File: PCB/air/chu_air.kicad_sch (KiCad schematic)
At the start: 24 parts, among them J1 Conn_01x06_Socket, Q1 Q_Photo_NPN, Q2 Q_Photo_NPN, Q3 Q_Photo_NPN, Q4 Q_Photo_NPN, Q5 Q_Photo_NPN, Q6 Q_Photo_NPN

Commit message: Another attempt of chu air
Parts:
- removed D10, D11, D12, D4, D5, D6, D7, D8, D9: IR26-21C_L110_TR8, LED_SMD:LED_1206_3216Metric_Pad1.42x1.75mm_HandSolder, symbol LED:IR26-21C_L110_TR8
- removed Q4, Q5, Q6: Q_Photo_NPN, LED_SMD:LED_1206_3216Metric_Pad1.42x1.75mm_HandSolder, symbol Device:Q_Photo_NPN
- removed R2: R, Resistor_SMD:R_0805_2012Metric_Pad1.20x1.40mm_HandSolder, symbol Device:R
- added J2: Conn_01x06_Socket, chu_air:6P_Air_Conn, symbol Connector:Conn_01x06_Socket
- added Q1, Q3, Q5: AO3400A, Package_TO_SOT_SMD:SOT-23, symbol Transistor_FET:AO3400A
- added R2, R4, R6: 1R, Resistor_SMD:R_0603_1608Metric, symbol Device:R_Small
- D1, D2, D3: footprint LED_SMD:LED_1206_3216Metric_Pad1.42x1.75mm_HandSolder -> LED_THT:LED_D5.0mm_IRGrey
- Q2: renamed from Q1; footprint LED_SMD:LED_1206_3216Metric_Pad1.42x1.75mm_HandSolder -> LED_THT:LED_D5.0mm_IRBlack
- Q4: renamed from Q2; footprint LED_SMD:LED_1206_3216Metric_Pad1.42x1.75mm_HandSolder -> LED_THT:LED_D5.0mm_IRBlack
- Q6: renamed from Q3; footprint LED_SMD:LED_1206_3216Metric_Pad1.42x1.75mm_HandSolder -> LED_THT:LED_D5.0mm_IRBlack
- R1, R3, R5: value R -> 10R; footprint Resistor_SMD:R_0805_2012Metric_Pad1.20x1.40mm_HandSolder -> Resistor_SMD:R_0603_1608Metric
- R7: renamed from R4; value R -> 10K; footprint Resistor_SMD:R_0805_2012Metric_Pad1.20x1.40mm_HandSolder -> Resistor_SMD:R_0603_1608Metric
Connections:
- net A: now also J2.1 (Pin_1)
- net B: now also J2.2 (Pin_2)
- net C: now also R5.1, J2.3 (Pin_3)
- net GND: now also J1.6 (Pin_6), J2.6 (Pin_6), Q1.2 (S), Q3.2 (S), Q5.2 (S); no longer J1.5 (Pin_5), R5.2
- net at R3.2: now also Q3.1 (G)
- net +3.3V: now reaches D3.2 (A)
- net +3.3V: now also D1.2 (A), D2.2 (A), J1.4 (Pin_4), J2.4 (Pin_4)
- net at D3.1 (K): now also R6.2
- net at D1.1 (K): now also R2.2
- net AD1 renamed SIG
- net SIG: now also J1.5 (Pin_5), J2.5 (Pin_5); no longer J1.6 (Pin_6)
- removed net AD2: J1.4 (Pin_4), R5.1
- new net: Q5.1 (G), R5.2
- new net: D2.1 (K), R4.2
- new net: Q3.3 (D), R4.1
- new net: Q1.1 (G), R1.2
- new net: Q5.3 (D), R6.1
- new net: Q1.3 (D), R2.1
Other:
- moved on the sheet: D1, J1, Q2, Q4, Q6, R7

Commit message: Air PCB v1.3
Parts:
- added C1, C2: 47uF, Capacitor_SMD:CP_Elec_5x5.9, symbol Device:C_Polarized
- added R7, R8, R9: 2K, Resistor_SMD:R_0603_1608Metric_Pad0.98x0.95mm_HandSolder, symbol Device:R_Small
- Q1, Q3, Q5: value AO3400A -> 2N7002
- R1, R2, R3, R4, R5, R6: footprint Resistor_SMD:R_0603_1608Metric -> Resistor_SMD:R_0603_1608Metric_Pad0.98x0.95mm_HandSolder
- R10: renamed from R7; footprint Resistor_SMD:R_0603_1608Metric -> Resistor_SMD:R_0603_1608Metric_Pad0.98x0.95mm_HandSolder
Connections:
- net +3.3V: now also C1.1, C2.1
- net A: now also R7.1
- net B: now also R8.1
- net C: now also R9.1
- net GND: now also C1.2, C2.2, R7.2, R8.2, R9.2

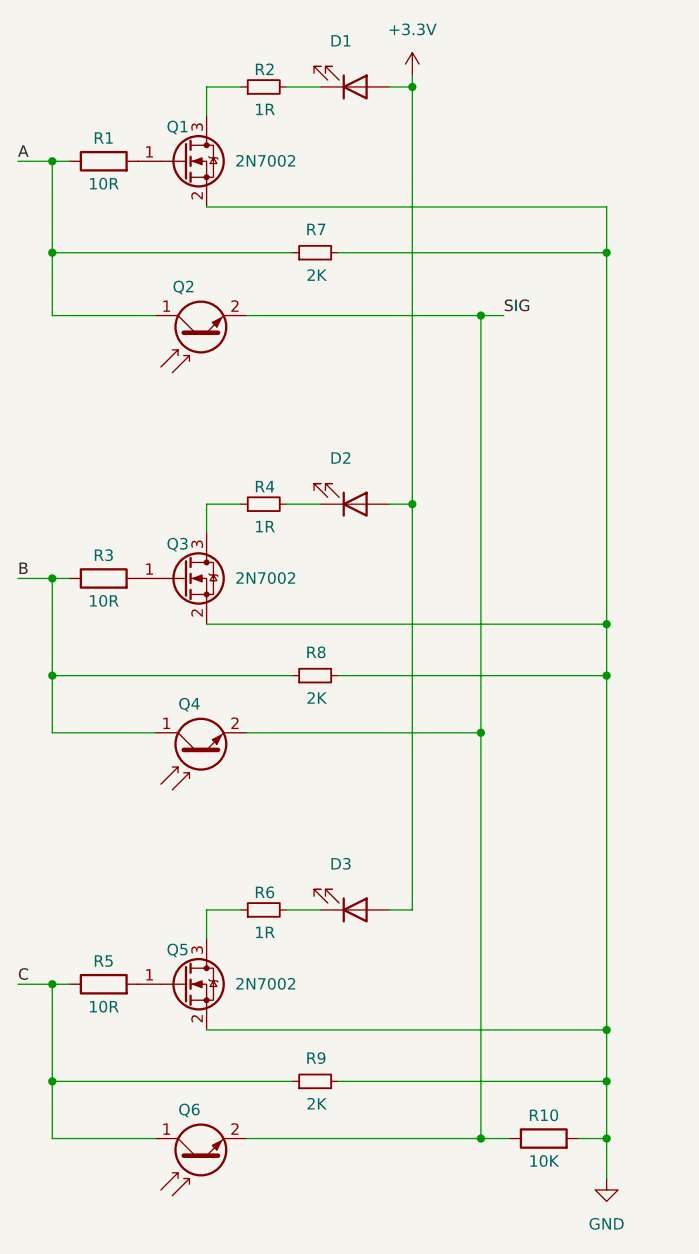
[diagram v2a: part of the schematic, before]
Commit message: Update component models in air PCB
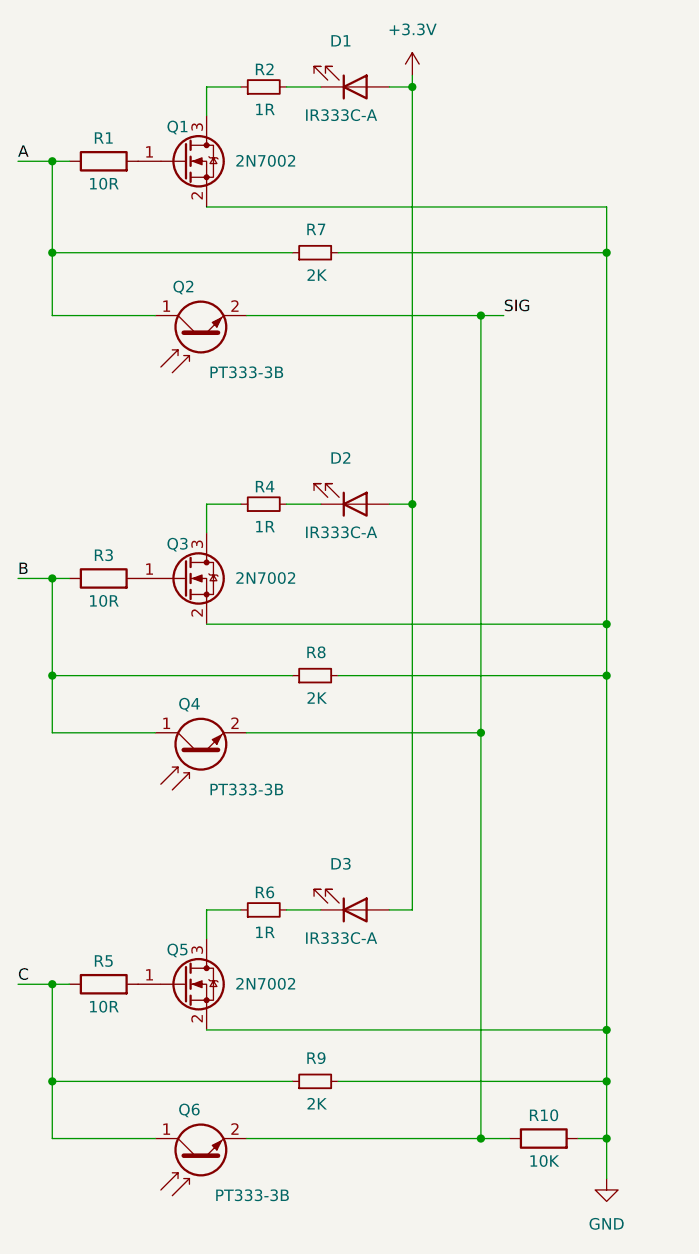
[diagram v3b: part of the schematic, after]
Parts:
- D1, D2, D3: value IR26-21C_L110_TR8 -> IR333C-A
- Q2, Q4, Q6: value Q_Photo_NPN -> PT333-3B
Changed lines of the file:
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@@
 			)
 		)
-		(property "Value" "IR26-21C_L110_TR8"
+		(property "Value" "IR333C-A"
 			(at 95.5675 93.345 0)
 			(effects
@@
 					(size 1.27 1.27)
 				)
-				(hide yes)
 			)
 		)
@@
 			)
 		)
-		(property "Value" "Q_Photo_NPN"
-			(at 79.2607 156.21 90)
-			(effects
-				(font
-					(size 1.27 1.27)
-				)
-				(hide yes)
+		(property "Value" "PT333-3B"
+			(at 85.725 167.005 90)
+			(effects
+				(font
+					(size 1.27 1.27)
+				)
 			)
 		)
@@
 			)
 		)
-		(property "Value" "Q_Photo_NPN"
-			(at 79.2607 64.77 90)
-			(effects
-				(font
-					(size 1.27 1.27)
-				)
-				(hide yes)
+		(property "Value" "PT333-3B"
+			(at 85.09 75.565 90)
+			(effects
+				(font
+					(size 1.27 1.27)
+				)
 			)
 		)
@@
 			)
 		)
-		(property "Value" "IR26-21C_L110_TR8"
+		(property "Value" "IR333C-A"
 			(at 95.5675 138.43 0)
 			(effects
@@
 					(size 1.27 1.27)
 				)
-				(hide yes)
 			)
 		)
@@
 			)
 		)
-		(property "Value" "IR26-21C_L110_TR8"
+		(property "Value" "IR333C-A"
 			(at 95.5675 46.99 0)
 			(effects
@@
 					(size 1.27 1.27)
 				)
-				(hide yes)
 			)
 		)
@@
 			)
 		)
-		(property "Value" "Q_Photo_NPN"
-			(at 79.2607 111.125 90)
-			(effects
-				(font
-					(size 1.27 1.27)
-				)
-				(hide yes)
-			)
-		)
+		(property "Value" "PT333-3B"
+			(at 85.09 121.92 90)
+			(effects
+				(font
+					(size 1.27 1.27)
+				)
+			)
+		)
